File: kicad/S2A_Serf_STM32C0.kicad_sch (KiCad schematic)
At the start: 17 parts, among them J1 Conn_01x02_Pin, J2 Conn_01x05_Socket, U2 STM32C011F6Px, U7 TXS0108E

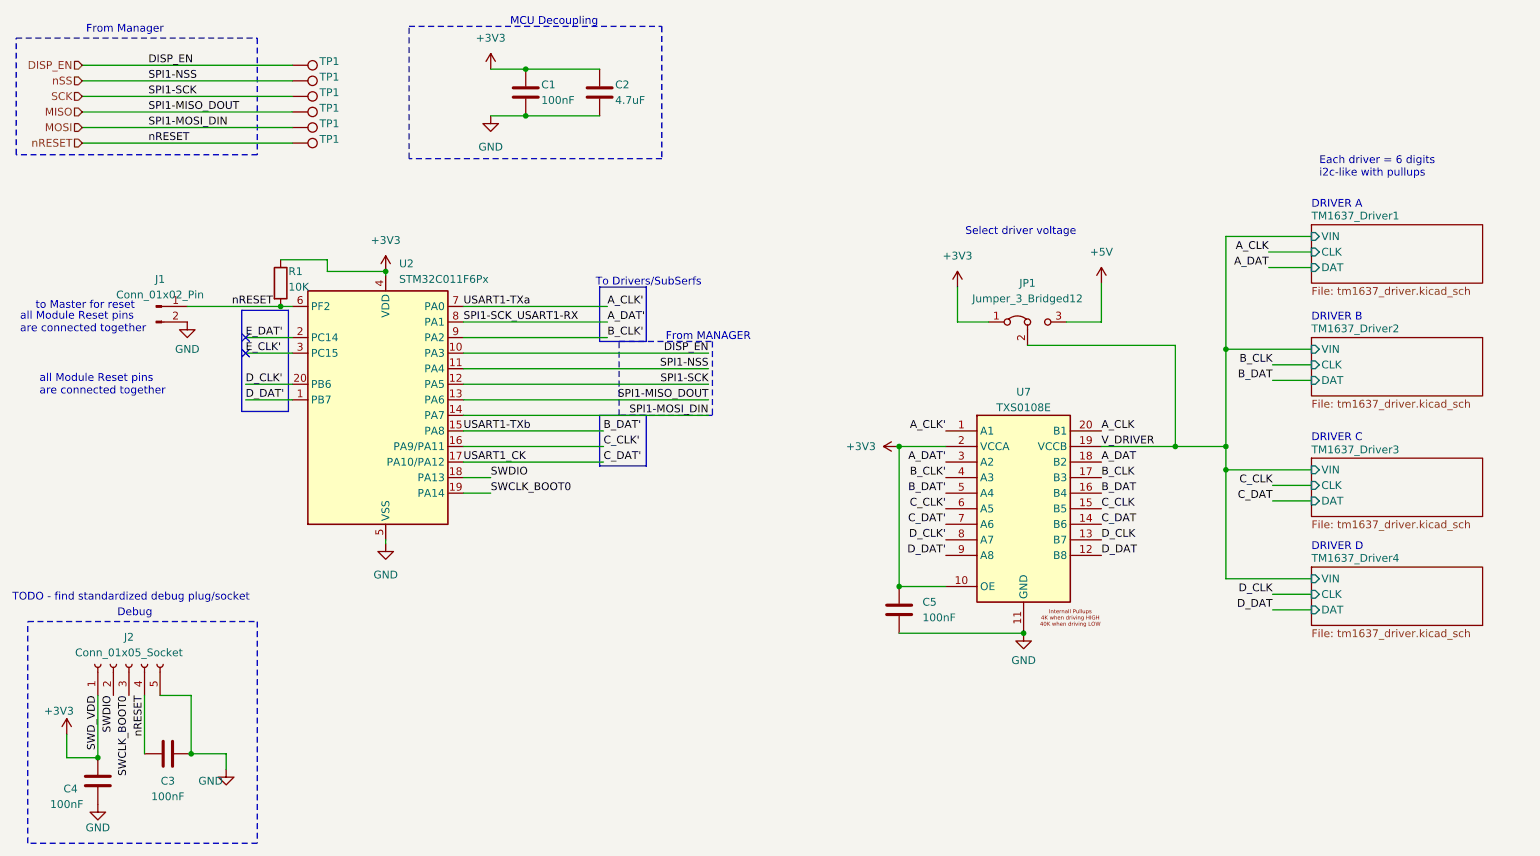
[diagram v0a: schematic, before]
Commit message: adding v-alpha prototype gerbers (note out of sync with kicad files)
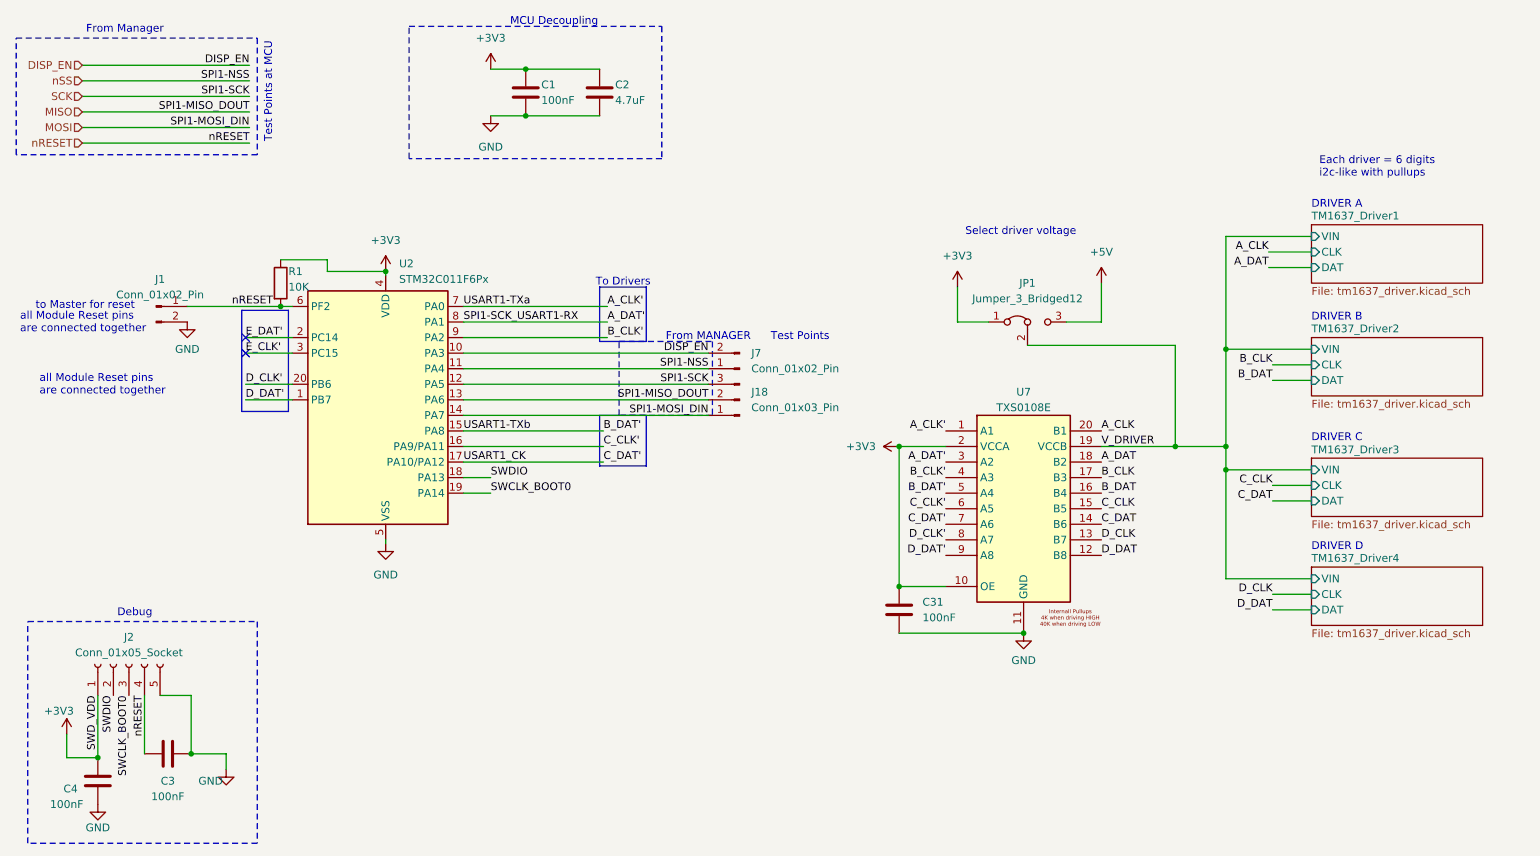
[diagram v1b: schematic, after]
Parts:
- removed TP1 (x6): TestPoint, symbol Connector:TestPoint
- added J18: Conn_01x03_Pin, Connector_PinHeader_1.27mm:PinHeader_1x03_P1.27mm_Vertical, symbol Connector:Conn_01x03_Pin
- added J7: Conn_01x02_Pin, Connector_PinHeader_1.27mm:PinHeader_1x02_P1.27mm_Vertical, symbol Connector:Conn_01x02_Pin
- C1, C3: footprint Capacitor_SMD:C_0805_2012Metric -> Capacitor_SMD:C_0603_1608Metric; Basic/Extended (none) -> Basic; DOUBLE_CHECK (none) -> x; JLPCB_MPN (none) -> CC0603KRX7R9BB104; JLPCB_Mfg (none) -> YAGEO; JLPCB_Part_No (none) -> C14663; JLPCB_Price (none) -> 0.0021; JLPCB_URL (none) -> https://jlcpcb.com/partdetail/Yageo-CC0603KRX7R9BB104/C14663; LCSC Part # (none) -> C14663
- C2: footprint Capacitor_SMD:C_0805_2012Metric -> Capacitor_SMD:C_0603_1608Metric; Basic/Extended (none) -> Basic; DOUBLE_CHECK (none) -> x; JLPCB_MPN (none) -> CL10A475KO8NNNC; JLPCB_Mfg (none) -> Samsung Electro-Mechanics; JLPCB_Part_No (none) -> C19666; JLPCB_Price (none) -> .0090; JLPCB_URL (none) -> https://jlcpcb.com/partdetail/20375-CL10A475KO8NNNC/C19666; LCSC Part # (none) -> C19666
- C31: renamed from C5; footprint (none) -> Capacitor_SMD:C_0603_1608Metric; Basic/Extended (none) -> Basic; DOUBLE_CHECK (none) -> x; JLPCB_MPN (none) -> CC0603KRX7R9BB104; JLPCB_Mfg (none) -> YAGEO; JLPCB_Part_No (none) -> C14663; JLPCB_Price (none) -> 0.0021; JLPCB_URL (none) -> https://jlcpcb.com/partdetail/Yageo-CC0603KRX7R9BB104/C14663; LCSC Part # (none) -> C14663
- C4: footprint Capacitor_SMD:C_0805_2012Metric -> Capacitor_SMD:C_0603_1608Metric; Basic/Extended B -> Basic; DOUBLE_CHECK (none) -> x; JLPCB_MPN CL05B104KO5NNNC -> CC0603KRX7R9BB104; JLPCB_Mfg Samsung Electro-Mechanics -> YAGEO; JLPCB_Part_No C1525 -> C14663; JLPCB_Price $0.0009 -> 0.0021; JLPCB_URL https://jlcpcb.com/partdetail/1877-CL05B104KO5NNNC/C1525 -> https://jlcpcb.com/partdetail/Yageo-CC0603KRX7R9BB104/C14663; LCSC Part # C1525 -> C14663
- J1: footprint Connector_PinHeader_1.27mm:PinHeader_1x02_P1.27mm_Vertical -> Connector_PinHeader_2.54mm:PinHeader_1x02_P2.54mm_Vertical; Basic/Extended (none) -> Extended; JLPCB_MPN (none) -> PZ254V-11-02P; JLPCB_Mfg (none) -> XFCN; JLPCB_Part_No (none) -> C492401; JLPCB_URL (none) -> https://jlcpcb.com/partdetail/Xfcn-PZ254V_1102P/C492401; LCSC Part # (none) -> C492401; now left out of the parts list
- J2: footprint Connector_PinHeader_1.27mm:PinHeader_1x05_P1.27mm_Vertical -> Connector_PinHeader_2.54mm:PinHeader_1x05_P2.54mm_Vertical; DNP (none) -> DNP
- R1: footprint Resistor_SMD:R_0805_2012Metric -> Resistor_SMD:R_0603_1608Metric; Basic/Extended (none) -> Basic; JLPCB_MPN (none) -> 0603WAF1002T5E; JLPCB_Mfg (none) -> UNI-ROYAL(Uniroyal Elec); JLPCB_Part_No (none) -> C25804; JLPCB_URL (none) -> https://jlcpcb.com/partdetail/26547-0603WAF1002T5E/C25804; LCSC Part # (none) -> C25804
- U2: Basic/Extended (none) -> Extended; DOUBLE_CHECK x -> TODO; JLPCB_MPN (none) -> STM32C011F6P6; JLPCB_Part_No (none) -> C5456198; JLPCB_Price (none) -> .768; JLPCB_URL (none) -> https://jlcpcb.com/partdetail/Stmicroelectronics-STM32C011F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; LCSC Part # (none) -> C5456198
- U7: footprint (none) -> Package_SO:TSSOP-20_4.4x6.5mm_P0.65mm; Basic/Extended (none) -> Extended; DOUBLE_CHECK (none) -> done, tsop-20 6.5x4.4 p0..65; DOUBLE_CHECK_SYMB (none) -> done; JLPCB_MPN (none) -> TXS0108EPWR; JLPCB_Part_No (none) -> C17206; JLPCB_Price (none) -> .3165; JLPCB_URL (none) -> https://jlcpcb.com/partdetail/TexasInstruments-TXS0108EPWR/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; LCSC Part # (none) -> C17206
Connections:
- net DISP_EN: now also J7.2 (Pin_2)
- net MISO: now also J18.2 (Pin_2)
- net MOSI: now also J18.1 (Pin_1)
- net SCK: now also J18.3 (Pin_3)
- net nSS: now also J7.1 (Pin_1)
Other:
- note added: "Test Points"
- note added: "Test Points at MCU"
- note added: "To Drivers"
- note removed: "TODO - find standardized debug plug/socket"
- note removed: "To Drivers/SubSerfs"
